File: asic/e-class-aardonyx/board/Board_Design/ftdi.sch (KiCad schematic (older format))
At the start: 60 parts, among them J1 USB_B_6PIN, J17 USB_OTG, J18 Conn_1x3_M, J2 Conn_1x8, J3 Conn_1x3_M, U1 FT2232H, U16 93LC56BT-I_OT, Y1 12MHz

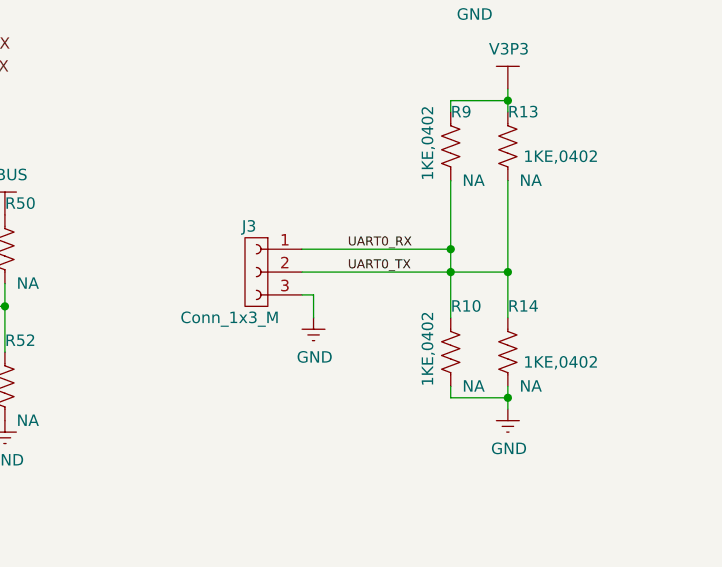
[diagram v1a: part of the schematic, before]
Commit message: update component placement
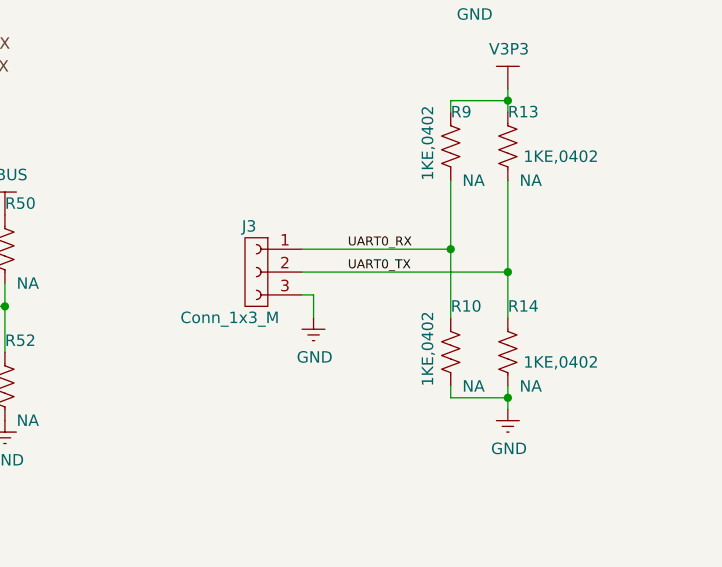
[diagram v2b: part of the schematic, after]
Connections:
- net UART0_RX: no longer J3.2 (Pin_2), R13.2, R14.1, R4.2
- new net UART0_TX: J3.2 (Pin_2), R13.2, R14.1, R4.2
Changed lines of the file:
@@
 	4650 1800 4650 1950
-Wire Wire Line
-	5150 2350 5150 1800
 Wire Wire Line
 	5150 1800 4950 1800
@@
 Wire Wire Line
 	10400 5450 10400 5650
-Wire Wire Line
-	9500 5450 10150 5450
-Wire Wire Line
-	10150 5450 10400 5450
 $Comp
 L Aardonyx-rescue:V3P3-aardonyx #PWR022
@@
 Text Label 9700 5350 0    39   ~ 0
 UART0_RX
-Wire Wire Line
-	10150 5350 10150 5450
 NoConn ~ 6850 3250
 NoConn ~ 6850 3350
@@
 NoConn ~ 6850 4650
 NoConn ~ 6850 4750
-NoConn ~ 6850 4850
-NoConn ~ 6850 4950
-NoConn ~ 6850 5050
-NoConn ~ 6850 5150
-NoConn ~ 6850 5350
 NoConn ~ 6850 5450
 NoConn ~ 6850 5550
@@
 	1    0    0    -1
 $EndComp
-$Comp
-L Aardonyx-rescue:FT2232H-aardonyx U1
-U 1 1 5DB6C49B
-P 5650 4550
-F 0 "U1" H 4650 6650 50  0000 C CNN
-F 1 "FT2232H" H 6550 2450 50  0000 C CNN
-F 2 "Package_QFP:LQFP-64_10x10mm_P0.5mm" H 5650 4550 50  0001 C CNN
-F 3 "https://www.digikey.com/product-detail/en/ftdi-future-technology-devices-international-ltd/FT2232HL-REEL/768-1024-1-ND/1986057" H 5650 4550 50  0001 C CNN
-F 4 "IC USB HS DUAL UART/FIFO 64-LQFP" H 5650 4550 50  0001 C CNN "Description"
-F 5 "768-1024-1-ND" H 5650 4550 50  0001 C CNN "Digikey PartNumber"
-F 6 "FT2232HL-REEL" H 5650 4550 50  0001 C CNN "Manufactured Part Number"
-F 7 "FTDI, Future Technology Devices International Ltd" H 5650 4550 50  0001 C CNN "Maufaturer"
-	1    5650 4550
-	1    0    0    -1
-$EndComp
 Wire Wire Line
 	1100 3450 900  3450
@@
 	1    0    0    -1
 $EndComp
-Connection ~ 10150 5450
-Wire Wire Line
-	10150 5450 10150 5650
 $Comp
 L Aardonyx-rescue:Conn_1x3_M-aardonyx J?
@@
 Wire Notes Line
 	650  3150 650  3000
+Wire Wire Line
+	5150 2350 5150 1800
+$Comp
+L Aardonyx-rescue:FT2232H-aardonyx U1
+U 1 1 5DB6C49B
+P 5650 4550
+F 0 "U1" H 4650 6650 50  0000 C CNN
+F 1 "FT2232H" H 6550 2450 50  0000 C CNN
+F 2 "Package_QFP:LQFP-64_10x10mm_P0.5mm" H 5650 4550 50  0001 C CNN
+F 3 "https://www.digikey.com/product-detail/en/ftdi-future-technology-devices-international-ltd/FT2232HL-REEL/768-1024-1-ND/1986057" H 5650 4550 50  0001 C CNN
+F 4 "IC USB HS DUAL UART/FIFO 64-LQFP" H 5650 4550 50  0001 C CNN "Description"
+F 5 "768-1024-1-ND" H 5650 4550 50  0001 C CNN "Digikey PartNumber"
+F 6 "FT2232HL-REEL" H 5650 4550 50  0001 C CNN "Manufactured Part Number"
+F 7 "FTDI, Future Technology Devices International Ltd" H 5650 4550 50  0001 C CNN "Maufaturer"
+	1    5650 4550
+	1    0    0    -1
+$EndComp
+NoConn ~ 6850 5350
+NoConn ~ 6850 5150
+NoConn ~ 6850 5050
+NoConn ~ 6850 4950
+NoConn ~ 6850 4850
+Wire Wire Line
+	9500 5450 10400 5450
+Wire Wire Line
+	10150 5350 10150 5650
 $EndSCHEMATC

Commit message: update foot print & componenet placement
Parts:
- Y1: footprint Crystal:Crystal_SMD_HC49-SD_HandSoldering -> Aardonyx:Crystal_SMD_ROHS_CSM_7XDN_HandSoldering
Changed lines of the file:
@@
 F 0 "Y1" H 3800 6418 50  0000 C CNN
 F 1 "12MHz" H 3800 6000 50  0000 C CNN
-F 2 "Crystal:Crystal_SMD_HC49-SD_HandSoldering" H 3800 6150 50  0001 C CNN
+F 2 "Aardonyx:Crystal_SMD_ROHS_CSM_7XDN_HandSoldering" H 3800 6150 50  0001 C CNN
 F 3 "https://www.digikey.in/product-detail/en/ecs-inc/ECS-120-20-5PXDN-TR/XC1298CT-ND/827762" H 3800 6150 50  0001 C CNN
 F 4 "9B-12.000MAAJ-B " H 3950 6300 50  0000 C CNN "Field4"

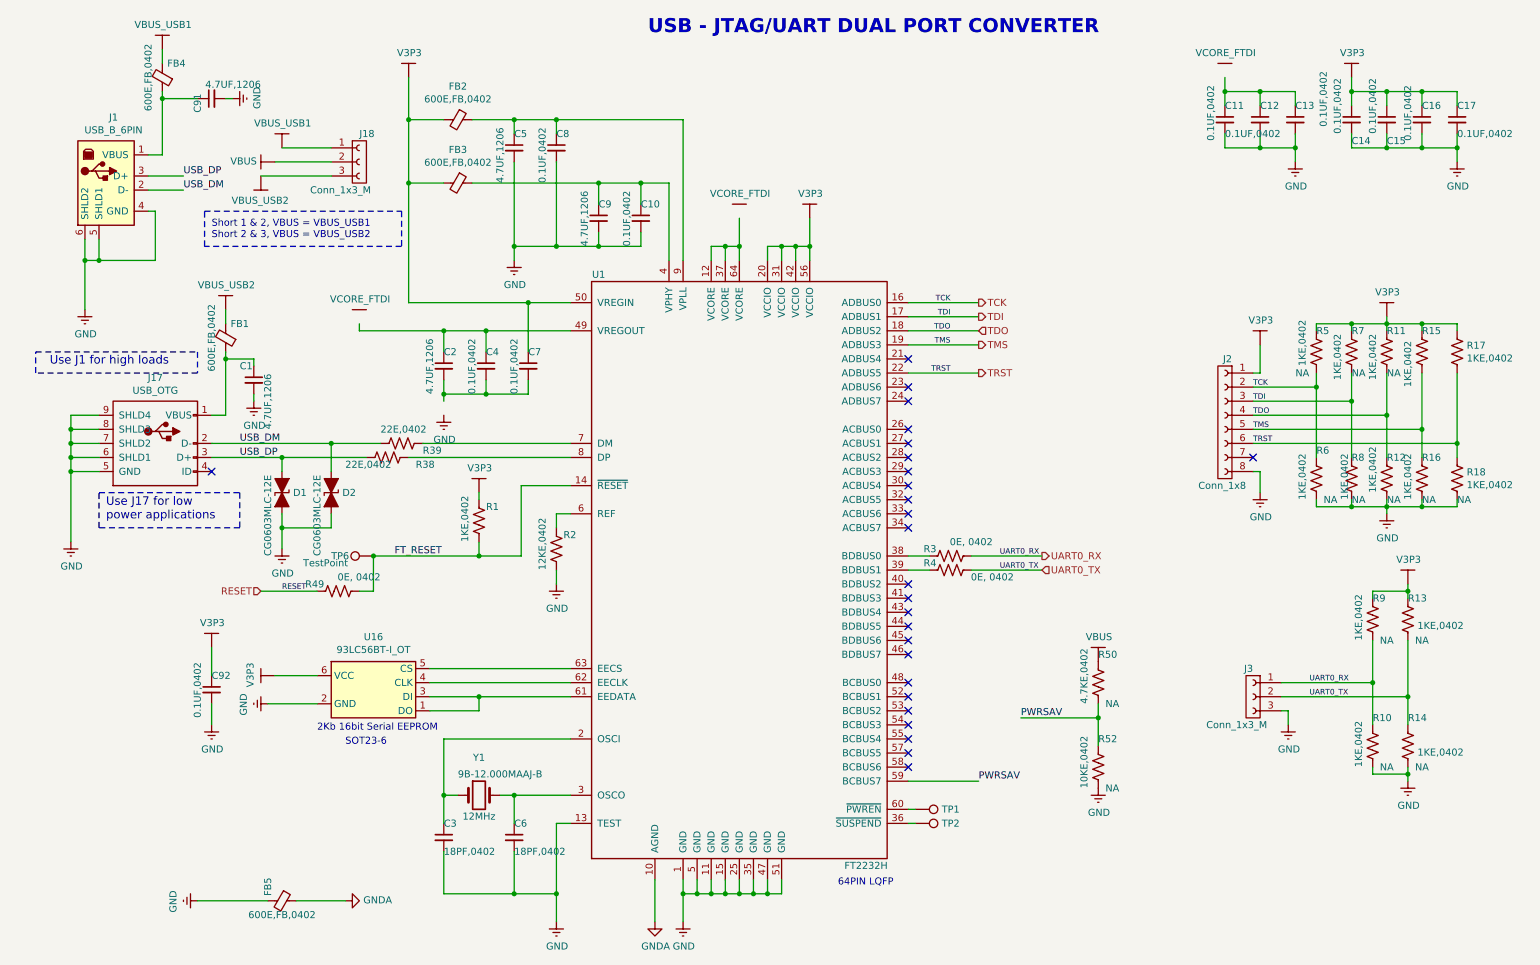
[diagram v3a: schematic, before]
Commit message: update component palcement comment by kottee
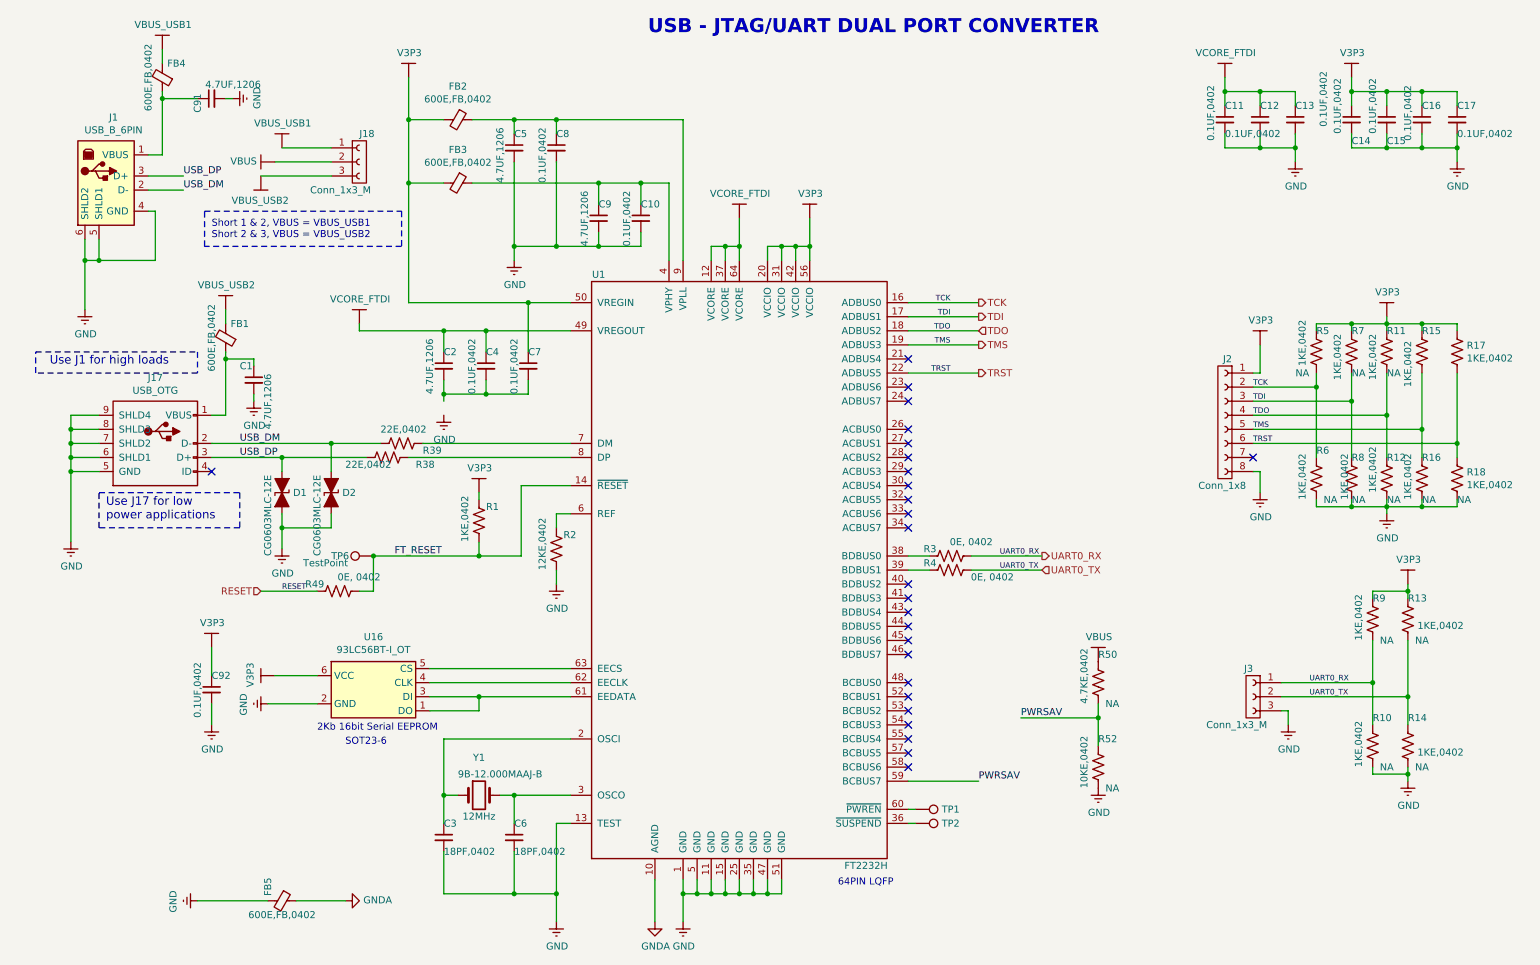
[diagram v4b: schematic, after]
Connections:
- net VBUS: no longer names the net of J18.2 (Pin_2)
- net VBUS: no longer R50.1
- net VBUS_USB1: no longer names the net of FB4.2
- net VBUS_USB1: no longer J18.1 (Pin_1)
- net VBUS_USB2: no longer names the net of FB1.2
- net VBUS_USB2: no longer J18.3 (Pin_3)
- removed net VCORE_FTDI: C11.1, C12.1, C13.1, C2.1, C4.1, U1.12 (VCORE), U1.37 (VCORE), U1.49 (VREGOUT), U1.64 (VCORE)
- new net: U1.12 (VCORE), U1.37 (VCORE), U1.64 (VCORE)
- new net: C2.1, C4.1, U1.49 (VREGOUT)
- new net: C11.1, C12.1, C13.1
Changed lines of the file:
@@
 $EndComp
 $Comp
-L Aardonyx-rescue:VCORE_FTDI-aardonyx #PWR04
+L Aardonyx-rescue:VCORE_FTDI-aardonyx-Aardonyx-rescue #PWR04
 U 1 1 5E3E23EC
 P 2950 2800
@@
 $EndComp
 $Comp
-L Aardonyx-rescue:VCORE_FTDI-aardonyx #PWR011
+L Aardonyx-rescue:VCORE_FTDI-aardonyx-Aardonyx-rescue #PWR011
 U 1 1 5E3E1553
 P 5650 2050
@@
 	9350 1550 9600 1550
 $Comp
-L Aardonyx-rescue:VCORE_FTDI-aardonyx #PWR013
+L Aardonyx-rescue:VCORE_FTDI-aardonyx-Aardonyx-rescue #PWR013
 U 1 1 5E454E04
 P 9100 1050
@@
 USB_DM
 $Comp
-L Aardonyx-rescue:VBUS_USB1 #PWR032
+L Aardonyx-rescue:VBUS_USB1-Aardonyx-rescue #PWR032
 U 1 1 5F2114E5
 P 1550 850
@@
 $EndComp
 $Comp
-L Aardonyx-rescue:VBUS_USB2 #PWR040
+L Aardonyx-rescue:VBUS_USB2-Aardonyx-rescue #PWR040
 U 1 1 5F2124AB
 P 2000 2700
@@
 	1700 1850 1450 1850
 $Comp
-L Aardonyx-rescue:VBUS_USB1 #PWR047
+L Aardonyx-rescue:VBUS_USB1-Aardonyx-rescue #PWR047
 U 1 1 5F343AAF
 P 2400 1550
@@
 	2400 1550 2750 1550
 $Comp
-L Aardonyx-rescue:VBUS_USB2 #PWR042
+L Aardonyx-rescue:VBUS_USB2-Aardonyx-rescue #PWR042
 U 1 1 5F345441
 P 2250 1750
@@
 $EndComp
 $Comp
-L Aardonyx-rescue:VBUS #PWR044
+L Aardonyx-rescue:VBUS-Aardonyx-rescue #PWR044
 U 1 1 5F3CB671
 P 2350 1650
@@
 $EndComp
 $Comp
-L Aardonyx-rescue:VBUS #PWR0164
+L Aardonyx-rescue:VBUS-Aardonyx-rescue #PWR0164
 U 1 1 5F511686
 P 8200 5200

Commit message: updated compo placement
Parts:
- TP1, TP2, TP6: footprint TestPoint:TestPoint_Bridge_Pitch2.54mm_Drill0.7mm -> Connector_PinHeader_2.54mm:PinHeader_1x01_P2.54mm_Vertical
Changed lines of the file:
@@
 F 0 "TP1" V 6900 6438 50  0000 L CNN
 F 1 "TestPoint" V 6945 6438 50  0001 L CNN
-F 2 "TestPoint:TestPoint_Bridge_Pitch2.54mm_Drill0.7mm" H 7100 6250 50  0001 C CNN
+F 2 "Connector_PinHeader_2.54mm:PinHeader_1x01_P2.54mm_Vertical" H 7100 6250 50  0001 C CNN
 F 3 "~" H 7100 6250 50  0001 C CNN
 	1    6900 6250
@@
 F 0 "TP2" V 6900 6538 50  0000 L CNN
 F 1 "TestPoint" V 6945 6538 50  0001 L CNN
-F 2 "TestPoint:TestPoint_Bridge_Pitch2.54mm_Drill0.7mm" H 7100 6350 50  0001 C CNN
+F 2 "Connector_PinHeader_2.54mm:PinHeader_1x01_P2.54mm_Vertical" H 7100 6350 50  0001 C CNN
 F 3 "~" H 7100 6350 50  0001 C CNN
 	1    6900 6350
@@
 F 0 "TP6" V 3050 4750 50  0000 R CNN
 F 1 "TestPoint" V 3000 4950 50  0000 R CNN
-F 2 "TestPoint:TestPoint_Bridge_Pitch2.54mm_Drill0.7mm" H 3250 4450 50  0001 C CNN
+F 2 "Connector_PinHeader_2.54mm:PinHeader_1x01_P2.54mm_Vertical" H 3250 4450 50  0001 C CNN
 F 3 "" H 3250 4450 50  0001 C CNN
 	1    3050 4450

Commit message: add bom
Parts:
- C1, C2, C5, C9, C91: Description CAP TANT 4.7UF 10% 16V 1206 -> CAP TANT 4.7UF 10% 16V 1206; Digikey PartNumber 399-3697-1-ND -> 399-18027-1-ND; Manufactured Part Number T491A475K016AT -> T491A475K016AT
- D1, D2: Description VARISTOR 0603 -> VARISTOR 0603; Manufactured Part Number CG0603MLC-12E -> CG0603MLC-12E; Maufaturer Bourns Inc. -> Bourns Inc.
- J1: Manufactured Part Number 61729-0010BLF -> 61729-0010BLF; Maufaturer Amphenol ICC (FCI) -> Amphenol ICC (FCI)
- J2: Digikey PartNumber 609-3264-ND -> 609-3264-ND
- R50: Digikey PartNumber 311-4.7KJRTR-ND -> 311-4.7KJRCT-ND
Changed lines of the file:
@@
 F 1 "4.7UF,1206" V 4550 1850 50  0000 L CNN
 F 2 "Capacitor_SMD:C_1206_3216Metric" H 4650 2050 50  0001 C CNN
-F 3 "https://www.digikey.in/product-detail/en/kemet/T491A475K016AT/399-3697-1-ND/819022" H 4650 2050 50  0001 C CNN
-F 4 "	CAP TANT 4.7UF 10% 16V 1206" H 4650 2050 50  0001 C CNN "Description"
-F 5 "	399-3697-1-ND" H 4650 2050 50  0001 C CNN "Digikey PartNumber"
-F 6 "	T491A475K016AT" H 4650 2050 50  0001 C CNN "Manufactured Part Number"
+F 3 "https://www.digikey.in/product-detail/en/kemet/T491A475K016AT/399-18027-1-ND/819022" H 4650 2050 50  0001 C CNN
+F 4 "CAP TANT 4.7UF 10% 16V 1206" H 4650 2050 50  0001 C CNN "Description"
+F 5 "399-18027-1-ND" H 4650 2050 50  0001 C CNN "Digikey PartNumber"
+F 6 "T491A475K016AT" H 4650 2050 50  0001 C CNN "Manufactured Part Number"
 F 7 "Kemet" H 4650 2050 50  0001 C CNN "Maufaturer"
 	1    4650 2050
@@
 F 1 "4.7UF,1206" V 3950 1300 50  0000 L CNN
 F 2 "Capacitor_SMD:C_1206_3216Metric" H 4050 1550 50  0001 C CNN
-F 3 "https://www.digikey.in/product-detail/en/kemet/T491A475K016AT/399-3697-1-ND/819022" H 4050 1550 50  0001 C CNN
-F 4 "	CAP TANT 4.7UF 10% 16V 1206" H 4050 1550 50  0001 C CNN "Description"
-F 5 "	399-3697-1-ND" H 4050 1550 50  0001 C CNN "Digikey PartNumber"
-F 6 "	T491A475K016AT" H 4050 1550 50  0001 C CNN "Manufactured Part Number"
+F 3 "https://www.digikey.in/product-detail/en/kemet/T491A475K016AT/399-18027-1-ND/819022" H 4050 1550 50  0001 C CNN
+F 4 "CAP TANT 4.7UF 10% 16V 1206" H 4050 1550 50  0001 C CNN "Description"
+F 5 "399-18027-1-ND" H 4050 1550 50  0001 C CNN "Digikey PartNumber"
+F 6 "T491A475K016AT" H 4050 1550 50  0001 C CNN "Manufactured Part Number"
 F 7 "Kemet" H 4050 1550 50  0001 C CNN "Maufaturer"
 	1    4050 1550
@@
 F 1 "4.7UF,1206" V 3450 2900 50  0000 L CNN
 F 2 "Capacitor_SMD:C_1206_3216Metric" H 3550 3100 50  0001 C CNN
-F 3 "https://www.digikey.in/product-detail/en/kemet/T491A475K016AT/399-3697-1-ND/819022" H 3550 3100 50  0001 C CNN
-F 4 "	CAP TANT 4.7UF 10% 16V 1206" H 3550 3100 50  0001 C CNN "Description"
-F 5 "	399-3697-1-ND" H 3550 3100 50  0001 C CNN "Digikey PartNumber"
-F 6 "	T491A475K016AT" H 3550 3100 50  0001 C CNN "Manufactured Part Number"
+F 3 "https://www.digikey.in/product-detail/en/kemet/T491A475K016AT/399-18027-1-ND/819022" H 3550 3100 50  0001 C CNN
+F 4 "CAP TANT 4.7UF 10% 16V 1206" H 3550 3100 50  0001 C CNN "Description"
+F 5 "399-18027-1-ND" H 3550 3100 50  0001 C CNN "Digikey PartNumber"
+F 6 "T491A475K016AT" H 3550 3100 50  0001 C CNN "Manufactured Part Number"
 F 7 "Kemet" H 3550 3100 50  0001 C CNN "Maufaturer"
 	1    3550 3100
@@
 F 1 "4.7UF,1206" V 2300 2850 50  0000 L CNN
 F 2 "Capacitor_SMD:C_1206_3216Metric" H 2200 3200 50  0001 C CNN
-F 3 "https://www.digikey.in/product-detail/en/kemet/T491A475K016AT/399-3697-1-ND/819022" H 2200 3200 50  0001 C CNN
-F 4 "	CAP TANT 4.7UF 10% 16V 1206" H 2200 3200 50  0001 C CNN "Description"
-F 5 "	399-3697-1-ND" H 2200 3200 50  0001 C CNN "Digikey PartNumber"
-F 6 "	T491A475K016AT" H 2200 3200 50  0001 C CNN "Manufactured Part Number"
+F 3 "https://www.digikey.in/product-detail/en/kemet/T491A475K016AT/399-18027-1-ND/819022" H 2200 3200 50  0001 C CNN
+F 4 "CAP TANT 4.7UF 10% 16V 1206" H 2200 3200 50  0001 C CNN "Description"
+F 5 "399-18027-1-ND" H 2200 3200 50  0001 C CNN "Digikey PartNumber"
+F 6 "T491A475K016AT" H 2200 3200 50  0001 C CNN "Manufactured Part Number"
 F 7 "Kemet" H 2200 3200 50  0001 C CNN "Maufaturer"
 	1    2200 3200
@@
 F 2 "Diode_SMD:D_0603_1608Metric" H 2400 4000 50  0001 C CNN
 F 3 "https://www.bourns.com/docs/Product-Datasheets/MLC.pdf" H 2400 4000 50  0001 C CNN
-F 4 "	VARISTOR 0603" H 2400 4000 50  0001 C CNN "Description"
+F 4 "VARISTOR 0603" H 2400 4000 50  0001 C CNN "Description"
 F 5 "CG0603MLC-12ECT-ND" H 2400 4000 50  0001 C CNN "Digikey PartNumber"
-F 6 "	CG0603MLC-12E" H 2400 4000 50  0001 C CNN "Manufactured Part Number"
-F 7 "	Bourns Inc." H 2400 4000 50  0001 C CNN "Maufaturer"
+F 6 "CG0603MLC-12E" H 2400 4000 50  0001 C CNN "Manufactured Part Number"
+F 7 "Bourns Inc." H 2400 4000 50  0001 C CNN "Maufaturer"
 	1    2400 4000
 	0    -1   1    0
@@
 F 2 "Diode_SMD:D_0603_1608Metric" H 2750 4000 50  0001 C CNN
 F 3 "https://www.bourns.com/docs/Product-Datasheets/MLC.pdf" H 2750 4000 50  0001 C CNN
-F 4 "	VARISTOR 0603" H 2750 4000 50  0001 C CNN "Description"
+F 4 "VARISTOR 0603" H 2750 4000 50  0001 C CNN "Description"
 F 5 "CG0603MLC-12ECT-ND" H 2750 4000 50  0001 C CNN "Digikey PartNumber"
-F 6 "	CG0603MLC-12E" H 2750 4000 50  0001 C CNN "Manufactured Part Number"
-F 7 "	Bourns Inc." H 2750 4000 50  0001 C CNN "Maufaturer"
+F 6 "CG0603MLC-12E" H 2750 4000 50  0001 C CNN "Manufactured Part Number"
+F 7 "Bourns Inc." H 2750 4000 50  0001 C CNN "Maufaturer"
 	1    2750 4000
 	0    -1   1    0
@@
 F 3 "https://www.digikey.com/products/en?keywords=68000-408HLF" H 9100 3450 50  0001 C CNN
 F 4 "CONN HEADER VERT 8POS 2.54MM" H 9100 3450 50  0001 C CNN "Description"
-F 5 "	609-3264-ND" H 9100 3450 50  0001 C CNN "Digikey PartNumber"
+F 5 "609-3264-ND" H 9100 3450 50  0001 C CNN "Digikey PartNumber"
 F 6 "68000-408HLF" H 9100 3450 50  0001 C CNN "Manufactured Part Number"
 F 7 "Amphenol ICC (FCI)" H 9100 3450 50  0001 C CNN "Maufaturer"
@@
 F 4 "CONN RCPT USB2.0 TYPEB 4POS R/A" H 1150 1800 50  0001 C CNN "Description"
 F 5 "609-1039-ND" H 1150 1800 50  0001 C CNN "Digikey PartNumber"
-F 6 "	61729-0010BLF" H 1150 1800 50  0001 C CNN "Manufactured Part Number"
-F 7 "	Amphenol ICC (FCI)" H 1150 1800 50  0001 C CNN "Maufaturer"
+F 6 "61729-0010BLF" H 1150 1800 50  0001 C CNN "Manufactured Part Number"
+F 7 "Amphenol ICC (FCI)" H 1150 1800 50  0001 C CNN "Maufaturer"
 	1    1150 1800
 	1    0    0    -1
@@
 F 1 "4.7UF,1206" V 2000 850 50  0000 L CNN
 F 2 "Capacitor_SMD:C_1206_3216Metric" H 1900 1200 50  0001 C CNN
-F 3 "https://www.digikey.in/product-detail/en/kemet/T491A475K016AT/399-3697-1-ND/819022" H 1900 1200 50  0001 C CNN
-F 4 "	CAP TANT 4.7UF 10% 16V 1206" H 1900 1200 50  0001 C CNN "Description"
-F 5 "	399-3697-1-ND" H 1900 1200 50  0001 C CNN "Digikey PartNumber"
-F 6 "	T491A475K016AT" H 1900 1200 50  0001 C CNN "Manufactured Part Number"
+F 3 "https://www.digikey.in/product-detail/en/kemet/T491A475K016AT/399-18027-1-ND/819022" H 1900 1200 50  0001 C CNN
+F 4 "CAP TANT 4.7UF 10% 16V 1206" H 1900 1200 50  0001 C CNN "Description"
+F 5 "399-18027-1-ND" H 1900 1200 50  0001 C CNN "Digikey PartNumber"
+F 6 "T491A475K016AT" H 1900 1200 50  0001 C CNN "Manufactured Part Number"
 F 7 "Kemet" H 1900 1200 50  0001 C CNN "Maufaturer"
 	1    1900 1200
@@
 F 1 "4.7KE,0402" V 8100 5200 50  0000 L CNN
 F 2 "Resistor_SMD:R_0402_1005Metric" V 8240 5340 50  0001 C CNN
-F 3 "https://www.digikey.in/product-detail/en/yageo/RC0402JR-074K7L/311-4-7KJRTR-ND/726477" H 8200 5350 50  0001 C CNN
+F 3 "https://www.digikey.in/product-detail/en/yageo/RC0402JR-074K7L/311-4-7KJRCT-ND/726477" H 8200 5350 50  0001 C CNN
 F 4 "NA" H 8300 5200 50  0000 C CNN "Field4"
 F 5 "RES SMD 4.7K OHM 5% 1/16W 0402" H 8200 5350 50  0001 C CNN "Description"
-F 6 "311-4.7KJRTR-ND" H 8200 5350 50  0001 C CNN "Digikey PartNumber"
+F 6 "311-4.7KJRCT-ND" H 8200 5350 50  0001 C CNN "Digikey PartNumber"
 F 7 "RC0402JR-074K7L" H 8200 5350 50  0001 C CNN "Manufactured Part Number"
 F 8 "Yageo" H 8200 5350 50  0001 C CNN "Maufaturer"
